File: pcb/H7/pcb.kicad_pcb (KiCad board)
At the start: 4 copper layers, 43 x 40.1 mm, 86 parts, among them u1 Comment, u2 Comment, u3 Comment, u4 Comment, u5 Comment, u6 Comment, u7 Comment, u8 Comment

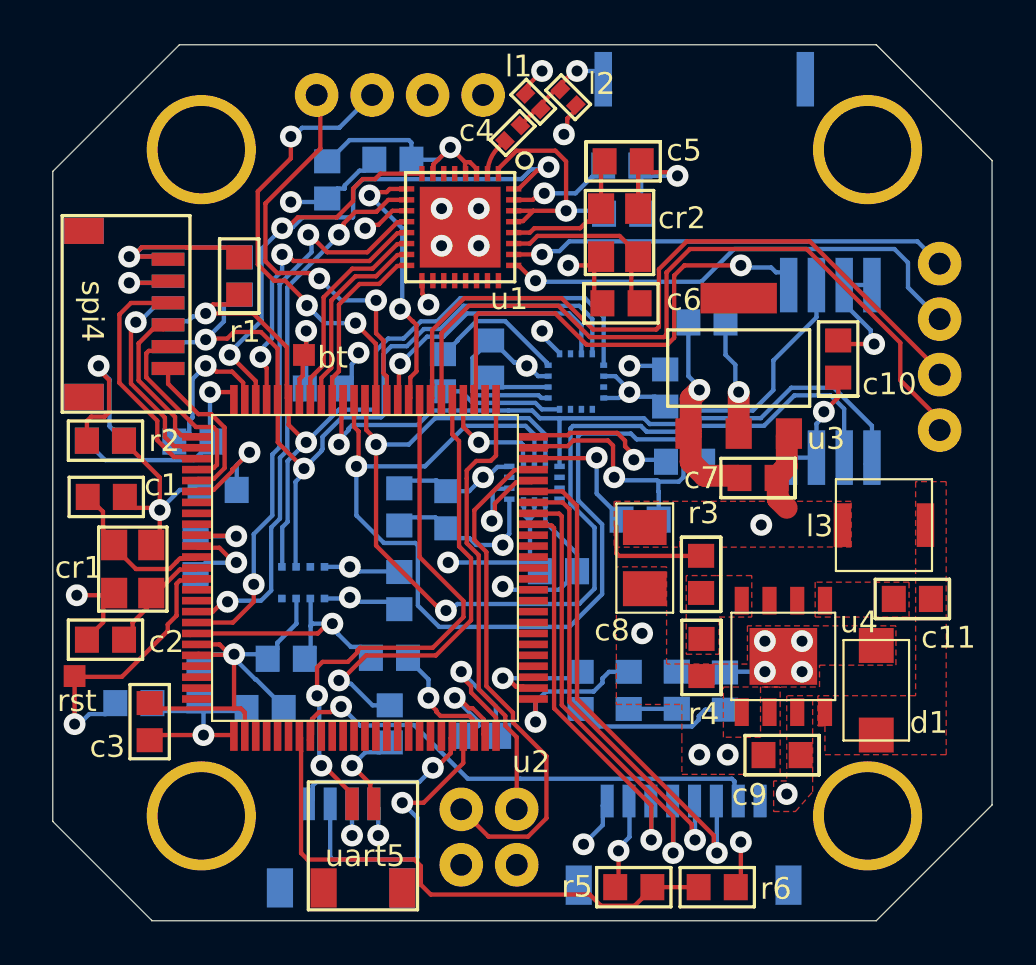
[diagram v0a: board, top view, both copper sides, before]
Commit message: switched to new board with imu and w25q on separate SPIs
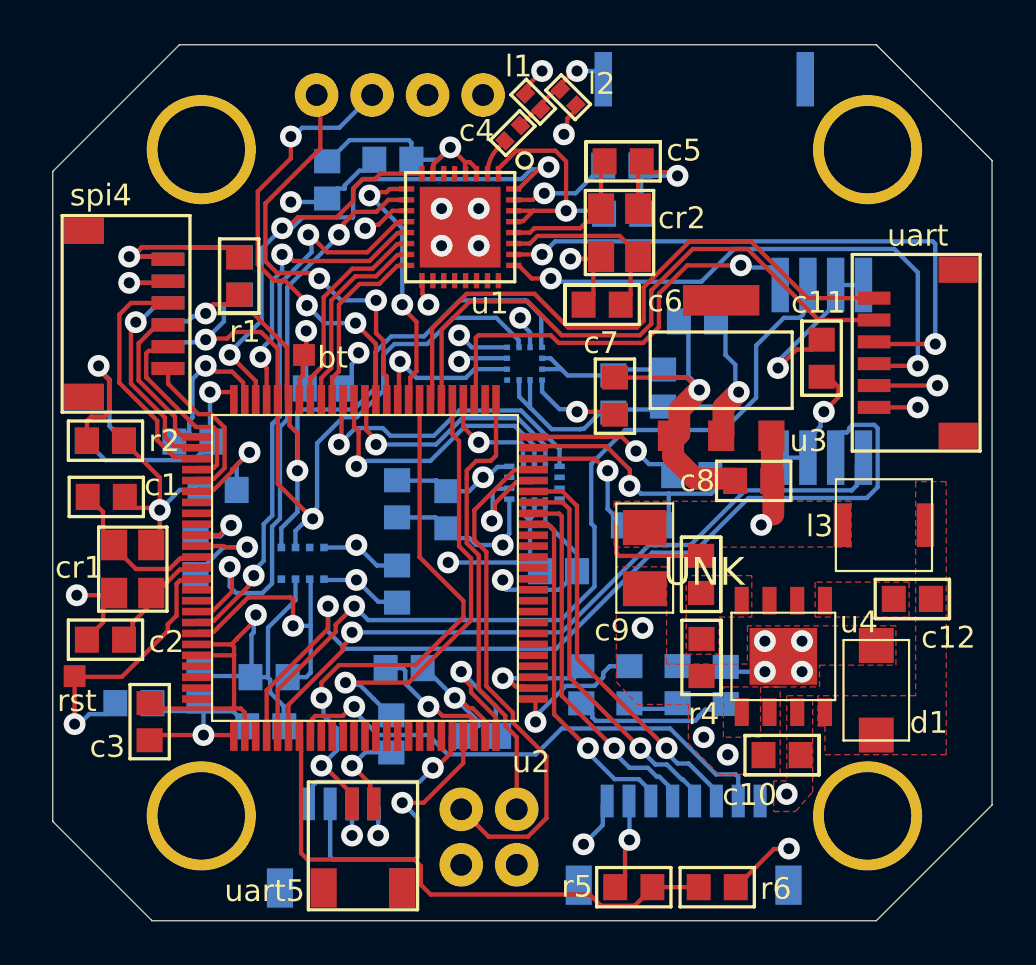
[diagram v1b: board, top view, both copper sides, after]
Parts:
- removed the ? at (167.6, 97.5)
- removed the ? at (167.6, 100.1)
- removed the ? at (167.6, 95.0)
- removed the ? at (167.6, 102.6)
- removed r3: Comment, PcbLib1:0603
- removed the uart at (140.1, 121.0)
- added UNK: 10 kOhm, PcbLib1:0603, F.Cu at (156.8, 109.1)
- added uart: JST SH-6, PcbLib1:SH1.0-6, F.Cu at (166.9, 100.2)
- added uart3: JST SH-4, PcbLib1:sh1.0-4, B.Cu at (140.1, 121.0)
- ant1: value Comment -> AN9520
- c1, c2, c5, c6: value Comment -> 18 pF
- c10, c20: value Comment -> 10 uF
- c11, c13, c14, c15, c17, c18, c19, c21, c22, c24, c26, c3, c30, c31, c7: value Comment -> 0.1 uF
- c12: value Comment -> 0.01 uF; moved to F.Cu
- c16, c27, c29: value Comment -> 1 uF
- c23, c25, c32: value Comment -> 2.2 uF
- c28: value Comment -> 4.7 uF
- c33: value Comment -> 0.01 uF
- c4: value Comment -> 5.6 pF, tdb
- c8: value Comment -> 1 uF; footprint PcbLib1:1206 -> PcbLib1:0603
- c9: value Comment -> 100 uF; footprint PcbLib1:0603 -> PcbLib1:1206
- cr1: value Comment -> 20 Mhz
- cr2: value Comment -> 40 Mhz
- d1: value Comment -> SS34
- esc: value Comment -> JST SH-8
- i2c1, spi4: value Comment -> JST SH-6
- l1, l2: value Comment -> tbd
- l3: value Comment -> 10 uH
- led1: value Comment -> orange LED
- led2: value Comment -> blue LED
- pwr: value Comment -> green LED
- r1, r5, r7: value Comment -> 3 kOhm
- r10: value Comment -> 12 kOhm
- r11, r12, r2: value Comment -> 1 kOhm
- r4: value Comment -> 3.3 kOhm
- r6: value Comment -> 6.8 kOhm
- r8: value Comment -> 10 kOhm
- r9: value Comment -> 100 Ohm
- u1: value Comment -> ESP8285
- u2: value Comment -> STMH723VGT6
- u3: value Comment -> LDL1117S33R
- u4: value Comment -> TPS5430DDAR
- u5: value Comment -> DPS368XTSA1
- u6: value Comment -> LIS3MDLTR; footprint PcbLib1:qmc5883l -> PcbLib1:lis3mdl
- u7: value Comment -> ICM-42688-P
- u8: value Comment -> W25Q128FVSIG
- uart5: value Comment -> JST SH-2
- moved c12 33.9 mm to (166.5, 110.5)
- moved c19 25.2 mm to (136.6, 116.3), turned to -90 degrees
- moved c27 24.8 mm to (153.2, 92.6)
- moved c10 18.3 mm to (160.5, 117.6), turned to -90 degrees
- moved c11 11.9 mm to (162.1, 99.4), turned to 180 degrees
- moved c9 11.8 mm to (153.3, 108.2)
- moved c21 10.3 mm to (142.5, 90.4), turned to -90 degrees
- moved c7 7.77 mm to (152.6, 101.2), turned to 180 degrees
- moved c17 7.56 mm to (130.6, 115.2), turned to -90 degrees
- moved c8 6.66 mm to (159.2, 105.1)
- moved c22 6.52 mm to (145.2, 106.4), turned to 0 degrees
- moved c28 6.11 mm to (156.4, 97.8), turned to -90 degrees
- moved c15 5.83 mm to (133.4, 108.2)
- moved c26 5.50 mm to (146.7, 116.5), turned to 90 degrees
- moved c29 5.18 mm to (152.8, 101.1), turned to 0 degrees
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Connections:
- c11 pad 1: dcdc_boot -> gnd
- c12 pad 1: gnd -> dcdc_boot
- c15 pad 1: vcc -> gnd
- c16 pad 1: nrst -> vcc
- c17 pad 1: gnd -> nrst
- c21 pad 1: qmc_c1 -> gnd
- c22 pad 1: qmc_setc -> vcc
- c25 pad 1: vcc -> gnd
- c26 pad 1: gnd -> vcc
- c27 pad 1: vcc -> gnd
- c29 pad 1: gnd -> vcc
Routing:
- net sck6: track 0.00 -> 43.5 mm, vias 0 -> 1
- net sck: track 56.5 -> 13.3 mm
- net mosi: track 53.6 -> 11.6 mm, vias 2 -> 1
- net miso6: track 0.00 -> 40.6 mm, vias 0 -> 1
- net mosi6: track 0.00 -> 33.2 mm, vias 0 -> 1
- net vcc: track 133.5 -> 153.4 mm
- net miso: track 31.6 -> 14.8 mm
- net gnd: track 147.4 -> 163.0 mm, vias 36 -> 37
- net rx4: track 35.9 -> 28.4 mm
- net esp_rx: track 20.2 -> 27.0 mm, vias 1 -> 2
- net qmc_setc: track 6.35 -> 0.00 mm
- net qmc_setp: track 5.68 -> 0.00 mm
- net drdy: track 12.5 -> 7.17 mm
- net tx4: track 33.5 -> 28.5 mm
- net ch4: track 23.2 -> 18.7 mm
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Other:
- board text removed: "erx"
- board text removed: "etx"
